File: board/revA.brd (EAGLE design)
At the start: 50 x 50 mm, 56 parts, among them IC1 74HCT125, Q1 VND7NV04, Q2 VND7NV04, Q3 VND7NV04, Q4 VND7NV04

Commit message: More routing tests
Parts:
- removed INJ: (no value), SparkFun-Connectors:1X04
- removed J1: (no value), SparkFun-Connectors:1X10
- added ANALOG, SENSOR: (no value), SparkFun-Connectors:MOLEX-1X3_LOCK
- added INJ_IN, INJ_OUT: (no value), SparkFun-Connectors:MOLEX-1X4_LOCK
- I2C: value B4B-ZR -> (none); device con-jst:B4B-ZR -> SparkFun-Connectors:MOLEX-1X4_LOCK
- R10, R7, R8, R9: device rcl:0207/7 -> rcl:0414/15
- UART: device SparkFun-Connectors:1X03 -> SparkFun-Connectors:MOLEX-1X3_LOCK
- moved IC1 35.1 mm to (8.00, 26.0)
- moved D5 13.0 mm to (14.0, 13.0)
- moved Q4 13.0 mm to (37.0, 38.0)
- moved C11 12.0 mm to (52.0, 20.0)
- moved R1 11.7 mm to (14.0, 20.0), turned to 0 degrees
- moved R6 11.7 mm to (14.0, 17.0), turned to 0 degrees
- moved D7 11.4 mm to (4.00, 13.0)
- moved Q2 11.4 mm to (21.0, 38.0)
- moved C10 11.0 mm to (49.0, 20.0)
- moved C15 11.0 mm to (39.0, 20.0)
- moved R11 10.2 mm to (57.0, 22.0)
- moved C4 10.0 mm to (57.0, 19.0), turned to 180 degrees
- moved C8 10.0 mm to (46.0, 20.0)
- moved R7 10.0 mm to (50.0, 51.0)
- moved SWD 10.0 mm to (57.5, 13.2)
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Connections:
- net N$5 renamed BUTTON
- net AN1: now also ANALOG.2; no longer J1.6
- net FF_SIG: now also SENSOR.2; no longer J1.8
- net GND: now also ANALOG.1, SENSOR.1; no longer J1.1, J1.7
- net I2C_SCL: now also I2C.3; no longer I2C.2
- net I2C_SDA: now also I2C.2; no longer I2C.3
- net INJ1: now also INJ_OUT.1, Q1.3; no longer J1.2, Q3.3
- net INJ1_IN: now also INJ_IN.1; no longer INJ.1
- net INJ2: now also INJ_OUT.2, Q2.3; no longer J1.3, Q4.3
- net INJ2_IN: now also INJ_IN.2; no longer INJ.2
- net INJ3: now also INJ_OUT.3, Q3.3; no longer J1.4, Q1.3
- net INJ3_IN: now also INJ_IN.3; no longer INJ.3
- net INJ3_TRIGGER: now also IC1.2; no longer IC1.5
- net INJ4: now also INJ_OUT.4, Q4.3; no longer J1.5, Q2.3
- net INJ4_IN: now also INJ_IN.4; no longer INJ.4
- net INJ4_TRIGGER: now also IC1.5; no longer IC1.2
- net N$10: now also IC1.3; no longer IC1.8
- net N$7: now also IC1.11; no longer IC1.3
- net N$8: now also IC1.8; no longer IC1.6
- net N$9: now also IC1.6; no longer IC1.11
- net SWCLK: now also SWD.3; no longer SWD.1
- net SWDIO: now also SWD.1; no longer SWD.3
- net VCC: now also ANALOG.3, SENSOR.3; no longer J1.10, J1.9
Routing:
- net INJ3_TRIGGER: track 12.1 -> 61.9 mm
- net +5V: track 75.4 -> 30.1 mm, vias 0 -> 2
- net VCC: track 105.6 -> 145.7 mm, vias 4 -> 3
- net INJ4_TRIGGER: track 14.7 -> 43.2 mm
- net INJ4: track 45.6 -> 19.1 mm
- net FF_SIG: track 68.1 -> 42.2 mm
- net INJ1_TRIGGER: track 14.9 -> 36.7 mm, vias 2 -> 4
- net INJ2_TRIGGER: track 17.1 -> 36.7 mm, vias 2 -> 4
- net AN_1: track 32.0 -> 50.0 mm, vias 2 -> 3
- net N$8: track 40.0 -> 22.0 mm, vias 4 -> 0
- net N$7: track 36.3 -> 22.5 mm
- net N$9: track 31.4 -> 44.2 mm, vias 4 -> 2
- net I2C_SCL: track 25.5 -> 13.0 mm, vias 1 -> 0
- net INJ4_IN: track 47.6 -> 58.2 mm, vias 1 -> 0
- net N$10: track 22.9 -> 33.0 mm
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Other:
- board size 50 x 50 mm -> 60 x 60 mm

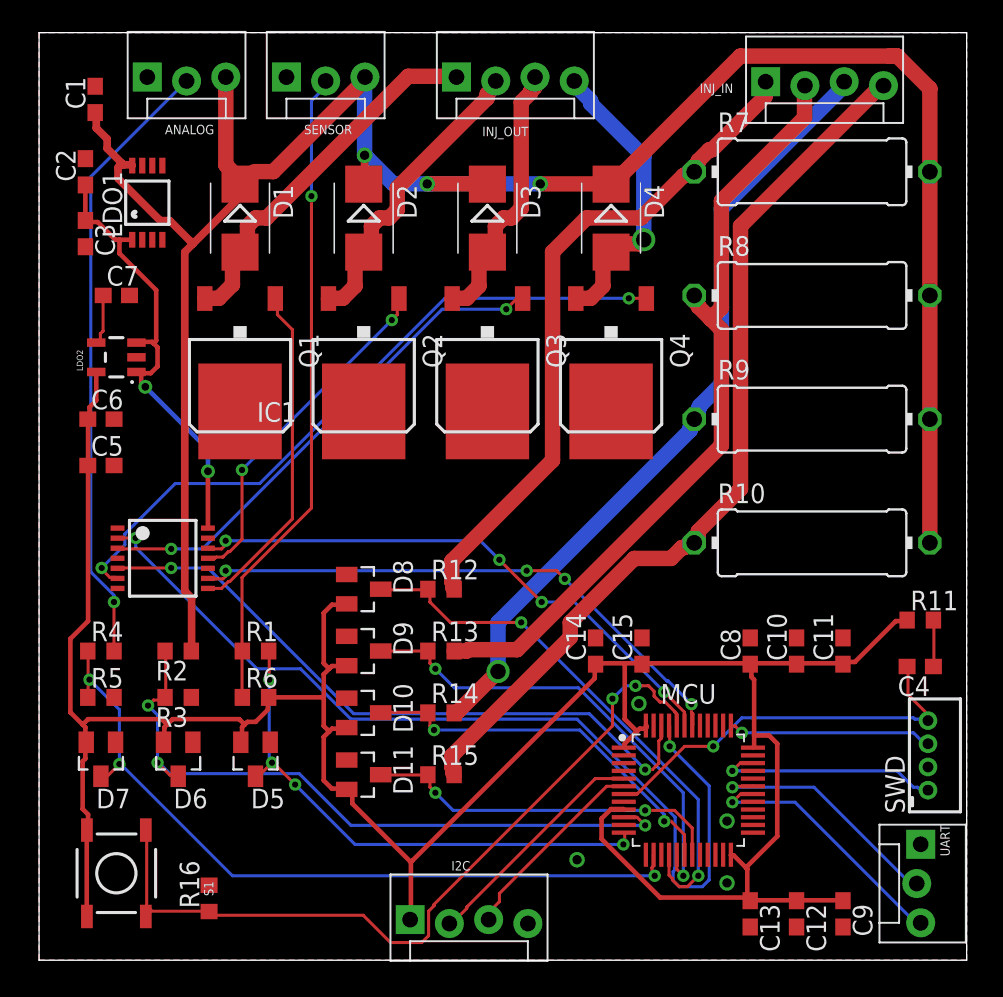
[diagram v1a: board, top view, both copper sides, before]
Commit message: Cleaning routing a bit
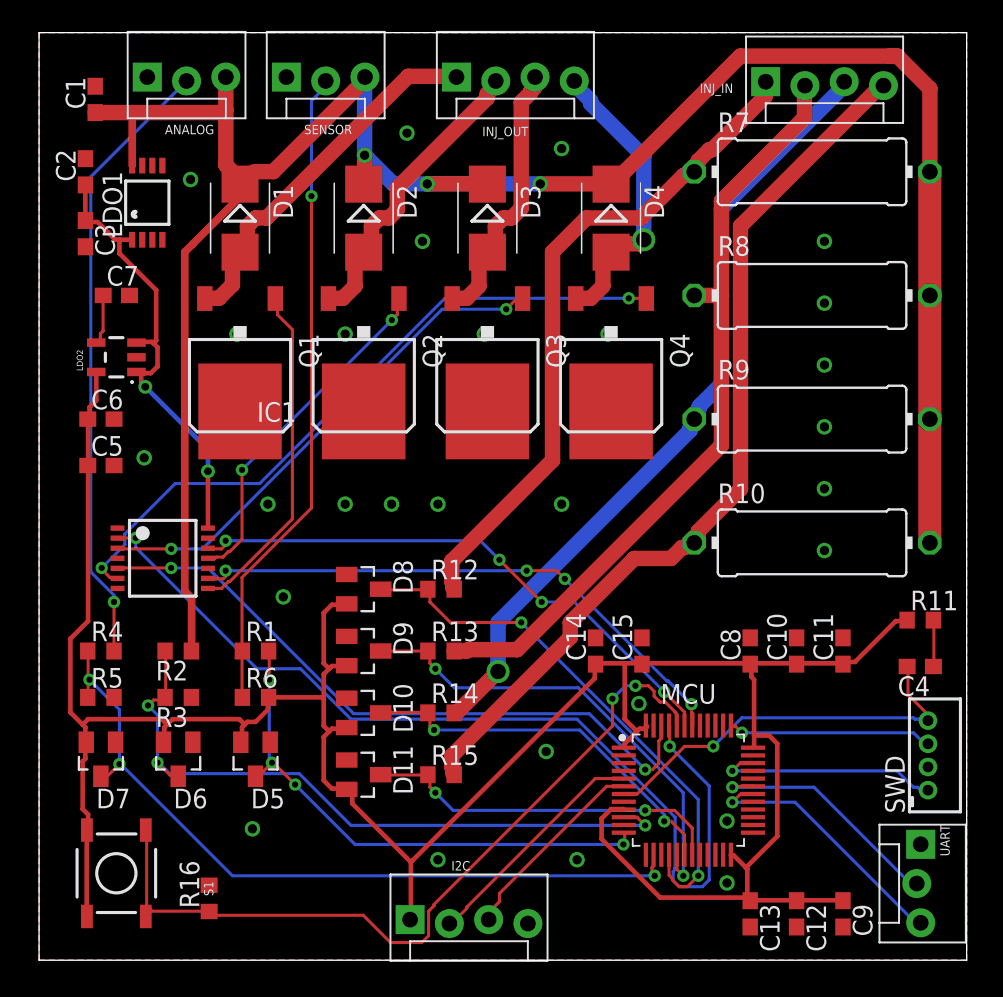
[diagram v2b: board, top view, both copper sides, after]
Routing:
- net INJ2_IN: track 51.2 -> 50.4 mm
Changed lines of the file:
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@@
 <via x="34.8" y="6.5" extent="1-16" drill="0.6"/>
 <via x="38.8" y="16.6" extent="1-16" drill="0.6"/>
+<via x="13.8" y="8.5" extent="1-16" drill="0.6"/>
+<via x="22.8" y="29.5" extent="1-16" drill="0.6"/>
+<via x="15.8" y="23.5" extent="1-16" drill="0.6"/>
+<via x="6.8" y="32.5" extent="1-16" drill="0.6"/>
+<via x="9.8" y="50.5" extent="1-16" drill="0.6"/>
+<via x="25.8" y="6.5" extent="1-16" drill="0.6"/>
+<via x="32.8" y="13.5" extent="1-16" drill="0.6"/>
+<via x="50.8" y="46.5" extent="1-16" drill="0.6"/>
+<via x="50.8" y="42.5" extent="1-16" drill="0.6"/>
+<via x="50.8" y="38.5" extent="1-16" drill="0.6"/>
+<via x="50.8" y="34.5" extent="1-16" drill="0.6"/>
+<via x="50.8" y="30.5" extent="1-16" drill="0.6"/>
+<via x="50.8" y="26.5" extent="1-16" drill="0.6"/>
+<via x="24.8" y="46.5" extent="1-16" drill="0.6"/>
+<via x="33.8" y="52.5" extent="1-16" drill="0.6"/>
+<via x="23.8" y="53.5" extent="1-16" drill="0.6"/>
+<via x="25.8" y="29.5" extent="1-16" drill="0.6"/>
+<via x="19.8" y="29.5" extent="1-16" drill="0.6"/>
+<via x="33.8" y="29.5" extent="1-16" drill="0.6"/>
+<via x="14.8" y="29.5" extent="1-16" drill="0.6"/>
+<via x="12.8" y="40.5" extent="1-16" drill="0.6"/>
+<via x="19.8" y="40.5" extent="1-16" drill="0.6"/>
+<via x="28.8" y="40.5" extent="1-16" drill="0.6"/>
+<via x="36.8" y="40.5" extent="1-16" drill="0.6"/>
 </signal>
 <signal name="VCC" class="3">
@@
 <contactref element="R10" pad="2"/>
 <contactref element="SENSOR" pad="3"/>
-<wire x1="21.0559" y1="52.0671" x2="21.0559" y2="50.217" width="0.5" layer="1"/>
+<wire x1="21.0559" y1="52.0671" x2="21.0559" y2="50.217" width="1" layer="1"/>
 <wire x1="21.0559" y1="50.217" x2="21" y2="50.2" width="0.5" layer="1"/>
 <wire x1="21.144" y1="57.0888" x2="21.08" y2="57.127" width="0.5" layer="16"/>
@@
 <wire x1="36.9139" y1="50.217" x2="37" y2="50.2" width="0.5" layer="1"/>
 <wire x1="25.2847" y1="50.217" x2="25.1085" y2="50.217" width="1" layer="16"/>
-<wire x1="5.4622" y1="51.4504" x2="5.9908" y2="51.4504" width="0.5" layer="1"/>
-<wire x1="4.405" y1="52.5076" x2="5.3741" y2="51.5385" width="0.5" layer="1"/>
-<wire x1="5.3741" y1="51.5385" x2="5.4622" y2="51.4504" width="0.5" layer="1"/>
-<wire x1="4.405" y1="53.1243" x2="4.405" y2="52.5076" width="0.5" layer="1"/>
-<wire x1="3.7002" y1="53.8291" x2="4.405" y2="53.1243" width="0.5" layer="1"/>
-<wire x1="3.7002" y1="54.7982" x2="3.7002" y2="53.8291" width="0.5" layer="1"/>
-<wire x1="5.9908" y1="51.4504" x2="6.025" y2="51.4" width="0.5" layer="1"/>
 <wire x1="3.7002" y1="54.7982" x2="3.63" y2="54.83" width="0.5" layer="1"/>
 <wire x1="9.8672" y1="23.4346" x2="9.8672" y2="20.0868" width="0.5" layer="1"/>
@@
 <wire x1="9.8672" y1="20.0868" x2="9.85" y2="20" width="0.5" layer="1"/>
 <wire x1="12.9507" y1="50.1289" x2="13" y2="50.2" width="0.5" layer="1"/>
-<wire x1="5.1098" y1="51.2742" x2="5.1979" y2="51.3623" width="0.5" layer="1"/>
-<wire x1="5.1098" y1="50.5694" x2="5.1098" y2="51.2742" width="0.5" layer="1"/>
-<wire x1="7.8409" y1="47.8383" x2="5.1098" y2="50.5694" width="0.5" layer="1"/>
-<wire x1="8.4576" y1="47.8383" x2="7.8409" y2="47.8383" width="0.5" layer="1"/>
-<wire x1="9.7791" y1="46.5168" x2="8.4576" y2="47.8383" width="0.5" layer="1"/>
-<wire x1="5.1979" y1="51.3623" x2="5.3741" y2="51.5385" width="0.5" layer="1"/>
-<wire x1="9.7791" y1="46.5168" x2="9.9553" y2="46.3406" width="0.5" layer="1"/>
 <wire x1="21.0559" y1="56.9126" x2="21.0559" y2="57.0888" width="1" layer="1"/>
 <wire x1="15.1532" y1="51.0099" x2="21.0559" y2="56.9126" width="1" layer="1"/>
@@
 <via x="25.1085" y="50.217" extent="1-16" drill="0.6"/>
 <via x="32.4208" y="50.217" extent="1-16" drill="0.6"/>
-<wire x1="57.62" y1="27" x2="57.62" y2="35" width="1" layer="1"/>
-<wire x1="57.62" y1="35" x2="57.62" y2="43" width="1" layer="1"/>
-<wire x1="57.62" y1="43" x2="57.62" y2="51" width="1" layer="1"/>
+<wire x1="57.62" y1="27" x2="57.62" y2="35" width="1.5" layer="1"/>
+<wire x1="57.62" y1="35" x2="57.62" y2="43" width="1.5" layer="1"/>
+<wire x1="57.62" y1="43" x2="57.62" y2="51" width="1.5" layer="1"/>
 <wire x1="57.62" y1="51" x2="57.62" y2="56.38" width="1" layer="1"/>
 <wire x1="57.62" y1="56.38" x2="55.516" y2="58.484" width="1" layer="1"/>
@@
 <wire x1="21.0559" y1="57.1029" x2="21.08" y2="57.127" width="1" layer="16"/>
 <contactref element="ANALOG" pad="3"/>
-<wire x1="12.08" y1="57.127" x2="12.08" y2="51.4401" width="1" layer="1"/>
+<wire x1="12.08" y1="57.127" x2="12.08" y2="55" width="1" layer="1"/>
+<wire x1="12.08" y1="55" x2="12.08" y2="51.4401" width="1" layer="1"/>
 <wire x1="12.08" y1="51.4401" x2="13.215" y2="50.3051" width="1" layer="1"/>
+<wire x1="3.63" y1="54.83" x2="6" y2="54.83" width="1" layer="1"/>
+<wire x1="6" y1="54.83" x2="11.91" y2="54.83" width="1" layer="1"/>
+<wire x1="11.91" y1="54.83" x2="12.08" y2="55" width="1" layer="1"/>
+<wire x1="6.025" y1="51.4" x2="6.025" y2="54.805" width="0.5" layer="1"/>
+<wire x1="6.025" y1="54.805" x2="6" y2="54.83" width="0.5" layer="1"/>
 </signal>
 <signal name="N$2">
@@
 <wire x1="27.7515" y1="20.0868" x2="27.6634" y2="19.9987" width="1" layer="1"/>
 <wire x1="30.9231" y1="20.0868" x2="27.7515" y2="20.0868" width="1" layer="1"/>
-<wire x1="44.1381" y1="33.3018" x2="30.9231" y2="20.0868" width="1" layer="1"/>
-<wire x1="44.1381" y1="40.7903" x2="44.1381" y2="33.3018" width="1" layer="1"/>
-<wire x1="42.6404" y1="42.288" x2="43.4333" y2="41.4951" width="1" layer="1"/>
-<wire x1="43.4333" y1="41.4951" x2="44.1381" y2="40.7903" width="1" layer="1"/>
-<wire x1="42.6404" y1="42.3761" x2="42.6404" y2="42.288" width="1" layer="1"/>
-<wire x1="42.288" y1="42.7285" x2="42.6404" y2="42.3761" width="1" layer="1"/>
-<wire x1="42.288" y1="42.9047" x2="42.288" y2="42.7285" width="1" layer="1"/>
-<wire x1="42.3761" y1="42.9928" x2="42.288" y2="42.9047" width="1" layer="1"/>
+<wire x1="30.9231" y1="20.0868" x2="44.1381" y2="33.3018" width="1" layer="1"/>
 <wire x1="26.8705" y1="19.9987" x2="26.85" y2="20" width="1" layer="1"/>
-<wire x1="42.3761" y1="42.9928" x2="42.38" y2="43" width="1" layer="1"/>
 <wire x1="49.5122" y1="54.4959" x2="49.5122" y2="56.8245" width="1" layer="1"/>
 <wire x1="44.1381" y1="49.1218" x2="49.5122" y2="54.4959" width="1" layer="1"/>
-<wire x1="44.1381" y1="42.1999" x2="44.1381" y2="49.1218" width="1" layer="1"/>
-<wire x1="43.7857" y1="41.8475" x2="44.1381" y2="42.1999" width="1" layer="1"/>
 <wire x1="49.5122" y1="56.8245" x2="49.54" y2="56.873" width="1" layer="1"/>
-<wire x1="43.7857" y1="41.8475" x2="43.4333" y2="41.4951" width="1" layer="1"/>
+<wire x1="44.1381" y1="33.3018" x2="44.1381" y2="43" width="1" layer="1"/>
+<wire x1="44.1381" y1="43" x2="44.1381" y2="49.1218" width="1" layer="1"/>
+<wire x1="42.38" y1="43" x2="44.1381" y2="43" width="1" layer="1"/>
 <wire x1="49.5122" y1="56.8245" x2="49.54" y2="56.573" width="0" layer="19" extent="1-1"/>
 </signal>

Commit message: Cleaning routing
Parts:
- IC1: device 74xx-eu:TSSOP14 -> misc:TSSOP14
- LDO1: value LM2931 -> LM2931-5.0; device national-semiconductor:MINI-SO8 -> national-semiconductor:SO08
- moved C1 0.61 mm to (3.03, 55.6)
- moved LDO1 0.54 mm to (6.80, 49.5)
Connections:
- net GND: now also LDO1.2, LDO1.3, LDO1.6
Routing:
- net BUTTON: track 51.8 -> 52.8 mm

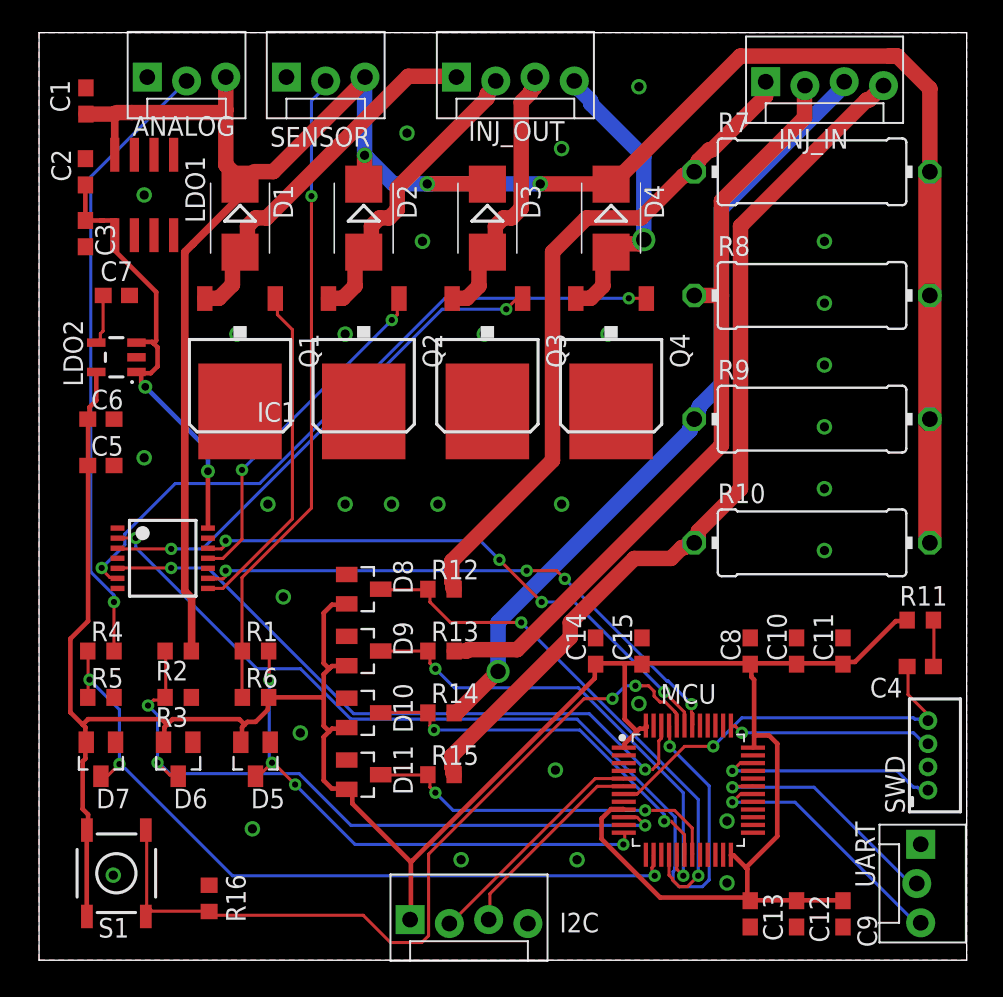
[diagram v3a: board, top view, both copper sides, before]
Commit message: Adding LED
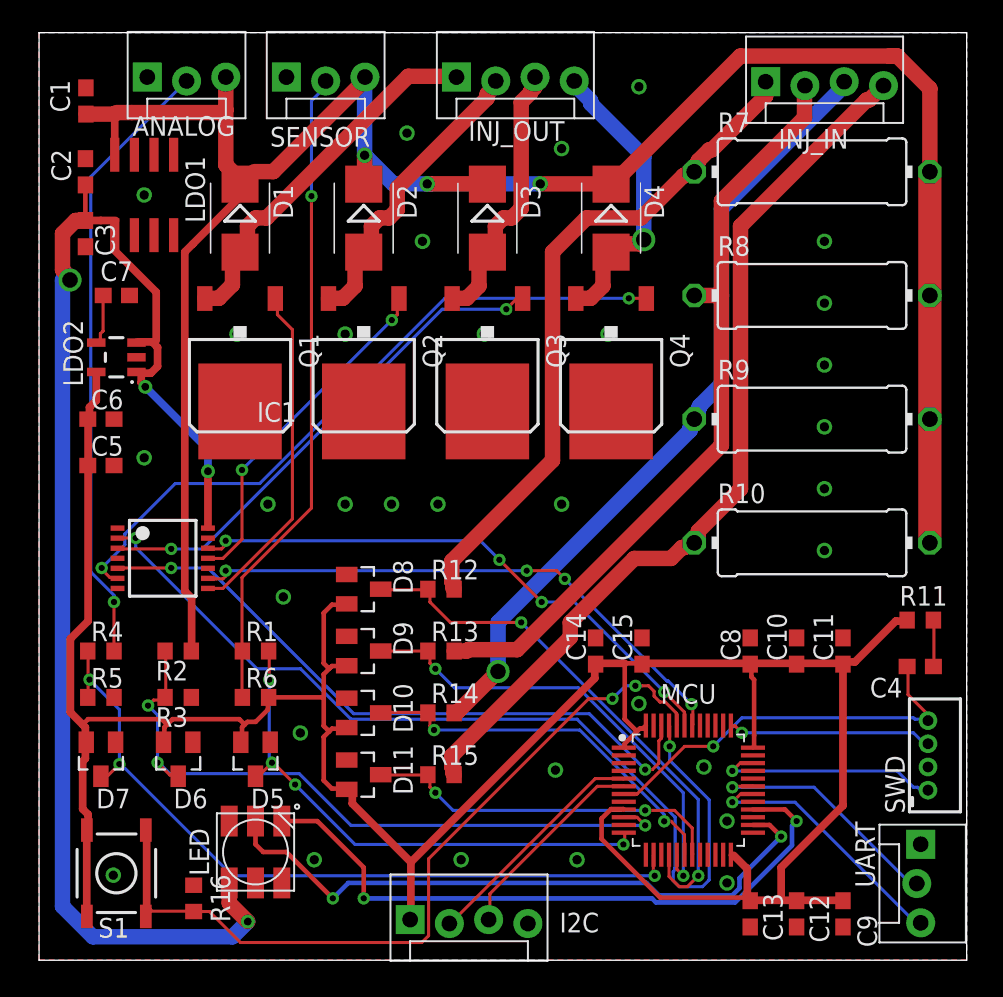
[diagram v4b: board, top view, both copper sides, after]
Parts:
- added LED: APA1025050, jos-ph:APA102_5050
- moved R16 1.00 mm to (10.0, 4.00)
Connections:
- net +5V: now also LED.1
- net GND: now also LED.6
- net SPI_MOSI: now also LED.4
- net SPI_SCK: now also LED.5
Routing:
- net +5V: track 30.3 -> 92.5 mm, vias 2 -> 4
- net SPI_MOSI: track 0.00 -> 42.7 mm, vias 0 -> 2
- net SPI_SCK: track 0.00 -> 41.8 mm, vias 0 -> 2
- net +3V3: track 170.3 -> 176.8 mm
